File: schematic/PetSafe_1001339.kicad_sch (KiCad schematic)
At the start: 148 parts, among them J1 ICSP, J3 PIR BOARD, J5 MOTOR, J6 DNP, Q1 FMOS3401A?, Q11 MMBTA55?, Q2 BC847B?, Q3 MMBTA55?, Q4 MMBTA55?, Q5 MMBTA55?, Q6 MMBTA55?, Q7 BC857C?, Q8 SIL3724A?, Q9 NPN option / DNP, U1 S-1200B45?, U106 U6A / LDO option, U2 SN74LVC2G14DBV?, U3 SGM8542XS, U4 PIC16F18855, U5 MX512H, U6 S-812C33AMC? / 3.3V, U7 DNP, Y1 20 MHz

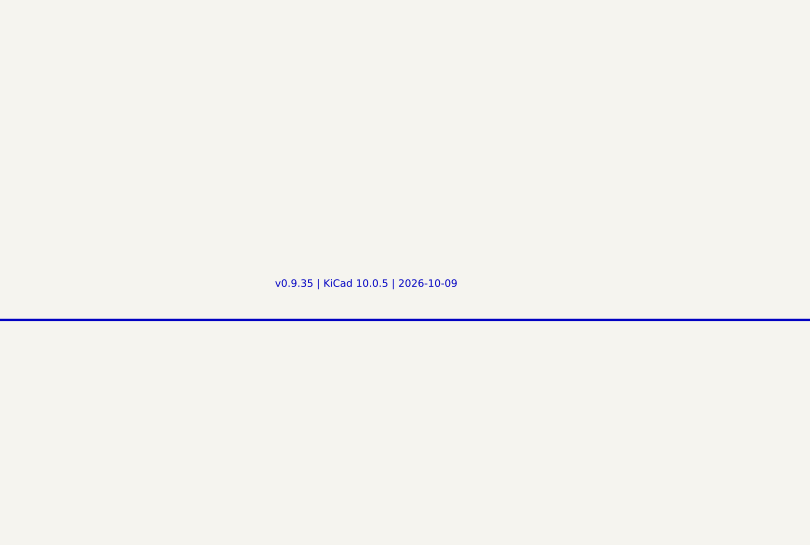
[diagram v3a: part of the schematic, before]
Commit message: Map J5 contacts and stage targeted antenna measurements
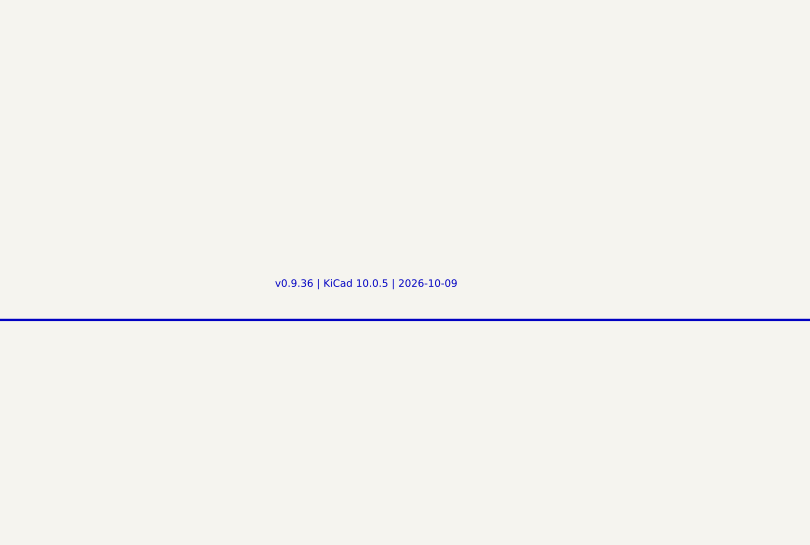
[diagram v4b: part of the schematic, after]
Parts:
- J5: CurrentEvidence (none) -> Photo-supported J5 map (IMG_2438 front, IMG_2439 rear): con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; Evidence Photo reconstruction; individual net evidence in reconstruc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 -> Photo-supported J5 map (IMG_2438 front, IMG_2439 rear): con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; PinMapping See evidence/pin_crosswalk.json; physical orientation may b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 -> Photo-supported J5 map (IMG_2438 front, IMG_2439 rear): con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
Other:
- note added: "v0.9.36 | KiCad 10.0.5 | 2026-10-09"
- note removed: "v0.9.35 | KiCad 10.0.5 | 2026-10-09"
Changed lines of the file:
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@@
 			)
 		)
+		(property "CurrentEvidence" "Photo-supported J5 map (IMG_2438 front, IMG_2439 rear): contact nearer C34 = A/native1 -> U5.8 OUTA; contact nearer BATTERY+ edge = B/native2 -> U5.5 OUTB/TP15. Connector body is on the rear. Harness colours, stock-footprint numbering and exact pitch remain unverified; no new bench result."
+			(at 499.11 62.23 0)
+			(effects
+				(font
+					(size 1.27 1.27)
+				)
+				(hide yes)
+			)
+		)
 		(pin "1"
 		)
@@
 				) hide)
 		)
-		(property "Evidence" "Photo reconstruction; individual net evidence in reconstruction.json"
+		(property "Evidence" "Photo-supported J5 map (IMG_2438 front, IMG_2439 rear): contact nearer C34 = A/native1 -> U5.8 OUTA; contact nearer BATTERY+ edge = B/native2 -> U5.5 OUTB/TP15. Connector body is on the rear. Harness colours, stock-footprint numbering and exact pitch remain unverified; no new bench result."
 			(at 499.11 62.23 0)
 			(effects
@@
 				) hide)
 		)
-		(property "PinMapping" "See evidence/pin_crosswalk.json; physical orientation may be provisional"
+		(property "PinMapping" "Photo-supported J5 map (IMG_2438 front, IMG_2439 rear): contact nearer C34 = A/native1 -> U5.8 OUTA; contact nearer BATTERY+ edge = B/native2 -> U5.5 OUTB/TP15. Connector body is on the rear. Harness colours, stock-footprint numbering and exact pitch remain unverified; no new bench result."
 			(at 499.11 62.23 0)
 			(effects
@@
 		)
 	)
-	(text "v0.9.35 | KiCad 10.0.5 | 2026-10-09"
+	(text "v0.9.36 | KiCad 10.0.5 | 2026-10-09"
 		(at 514.35 370.84000000000003 0)
 		(effects
@@
 	)
 	(junction
-		(at 430.53 87.63)
+		(at 455.93 87.63)
 		(diameter 0)
 		(color 0 0 0 0)
 	)
 	(junction
-		(at 455.93 87.63)
+		(at 461.01 87.63)
 		(diameter 0)
 		(color 0 0 0 0)
 	)
 	(junction
-		(at 114.3 298.45)
+		(at 330.2 326.39)
 		(diameter 0)
 		(color 0 0 0 0)
 	)
 	(junction
-		(at 330.2 326.39)
+		(at 262.89 132.08)
 		(diameter 0)
 		(color 0 0 0 0)
 	)
 	(junction
-		(at 55.88 81.28)
+		(at 302.26 132.08)
 		(diameter 0)
 		(color 0 0 0 0)
 	)
 	(junction
-		(at 83.82 81.28)
+		(at 114.3 81.28)
 		(diameter 0)
 		(color 0 0 0 0)
 	)
 	(junction
-		(at 262.89 132.08)
+		(at 430.53 87.63)
 		(diameter 0)
 		(color 0 0 0 0)
 	)
 	(junction
-		(at 302.26 132.08)
+		(at 55.88 81.28)
 		(diameter 0)
 		(color 0 0 0 0)
 	)
 	(junction
-		(at 461.01 87.63)
+		(at 528.32 87.63)
 		(diameter 0)
 		(color 0 0 0 0)
 	)
 	(junction
-		(at 114.3 81.28)
+		(at 342.9 52.07)
 		(diameter 0)
 		(color 0 0 0 0)
 	)
 	(junction
-		(at 342.9 52.07)
+		(at 213.36 364.49)
 		(diameter 0)
 		(color 0 0 0 0)
@@
 	)
 	(junction
-		(at 134.62 81.28)
+		(at 220.98 298.45)
 		(diameter 0)
 		(color 0 0 0 0)
 	)
 	(junction
-		(at 220.98 298.45)
+		(at 134.62 81.28)
 		(diameter 0)
 		(color 0 0 0 0)
 	)
 	(junction
-		(at 99.06 298.45)
+		(at 152.4 298.45)
 		(diameter 0)
 		(color 0 0 0 0)
@@
 	)
 	(junction
-		(at 213.36 364.49)
+		(at 259.08 298.45)
 		(diameter 0)
 		(color 0 0 0 0)
 	)
 	(junction
-		(at 259.08 298.45)
+		(at 114.3 298.45)
 		(diameter 0)
 		(color 0 0 0 0)
 	)
 	(junction
-		(at 152.4 298.45)
+		(at 60.96 298.45)
 		(diameter 0)
 		(color 0 0 0 0)
 	)
 	(junction
-		(at 60.96 298.45)
+		(at 83.82 81.28)
 		(diameter 0)
 		(color 0 0 0 0)
@@
 	)
 	(junction
-		(at 322.58 132.08)
+		(at 99.06 298.45)
 		(diameter 0)
 		(color 0 0 0 0)
 	)
 	(junction
-		(at 528.32 87.63)
+		(at 322.58 132.08)
 		(diameter 0)
 		(color 0 0 0 0)
 	)
 	(junction
-		(at 445.77 250.19)
+		(at 481.33 104.14)
 		(diameter 0)
 		(color 0 0 0 0)
 	)
 	(junction
-		(at 360.68 198.12)
+		(at 114.3 53.34)
 		(diameter 0)
 		(color 0 0 0 0)
 	)
 	(junction
-		(at 502.92 180.34)
+		(at 134.62 53.34)
 		(diameter 0)
 		(color 0 0 0 0)
 	)
 	(junction
-		(at 502.92 200.66)
+		(at 322.58 113.03)
 		(diameter 0)
 		(color 0 0 0 0)
 	)
 	(junction
-		(at 106.68 322.58)
+		(at 22.86 210.82)
 		(diameter 0)
 		(color 0 0 0 0)
 	)
 	(junction
-		(at 322.58 113.03)
+		(at 22.86 226.06)
 		(diameter 0)
 		(color 0 0 0 0)
 	)
 	(junction
-		(at 114.3 53.34)
+		(at 22.86 251.46)
 		(diameter 0)
 		(color 0 0 0 0)
 	)
 	(junction
-		(at 134.62 53.34)
+		(at 300.99 182.88)
 		(diameter 0)
 		(color 0 0 0 0)
 	)
 	(junction
-		(at 123.19 102.87)
+		(at 314.96 302.26)
 		(diameter 0)
 		(color 0 0 0 0)
 	)
 	(junction
-		(at 101.6 102.87)
+		(at 388.62 327.66)
 		(diameter 0)
 		(color 0 0 0 0)
 	)
 	(junction
-		(at 91.44 102.87)
+		(at 349.25 182.88)
 		(diameter 0)
 		(color 0 0 0 0)
 	)
 	(junction
-		(at 488.95 237.49)
+		(at 266.7 322.58)
 		(diameter 0)
 		(color 0 0 0 0)
 	)
 	(junction
-		(at 48.26 53.34)
+		(at 483.87 69.85)
 		(diameter 0)
 		(color 0 0 0 0)
 	)
 	(junction
-		(at 55.88 53.34)
+		(at 488.95 237.49)
 		(diameter 0)
 		(color 0 0 0 0)
 	)
 	(junction
-		(at 66.04 53.34)
+		(at 106.68 322.58)
 		(diameter 0)
 		(color 0 0 0 0)
 	)
 	(junction
-		(at 349.25 182.88)
+		(at 67.31 217.17)
 		(diameter 0)
 		(color 0 0 0 0)
 	)
 	(junction
-		(at 53.34 322.58)
+		(at 38.1 217.17)
 		(diameter 0)
 		(color 0 0 0 0)
 	)
 	(junction
-		(at 300.99 182.88)
+		(at 360.68 198.12)
 		(diameter 0)
 		(color 0 0 0 0)
 	)
 	(junction
-		(at 302.26 113.03)
+		(at 445.77 250.19)
 		(diameter 0)
 		(color 0 0 0 0)
 	)
 	(junction
-		(at 481.33 104.14)
+		(at 48.26 53.34)
 		(diameter 0)
 		(color 0 0 0 0)
 	)
 	(junction
-		(at 558.8 58.42)
+		(at 55.88 53.34)
 		(diameter 0)
 		(color 0 0 0 0)
 	)
 	(junction
-		(at 213.36 322.58)
+		(at 66.04 53.34)
 		(diameter 0)
 		(color 0 0 0 0)
 	)
 	(junction
-		(at 388.62 327.66)
+		(at 91.44 102.87)
 		(diameter 0)
 		(color 0 0 0 0)
 	)
 	(junction
-		(at 22.86 210.82)
+		(at 101.6 102.87)
 		(diameter 0)
 		(color 0 0 0 0)
 	)
 	(junction
-		(at 22.86 226.06)
+		(at 123.19 102.87)
 		(diameter 0)
 		(color 0 0 0 0)
 	)
 	(junction
-		(at 22.86 251.46)
+		(at 213.36 322.58)
 		(diameter 0)
 		(color 0 0 0 0)
 	)
 	(junction
-		(at 377.19 231.14)
+		(at 237.49 167.64)
 		(diameter 0)
 		(color 0 0 0 0)
 	)
 	(junction
-		(at 469.9 180.34)
+		(at 302.26 113.03)
 		(diameter 0)
 		(color 0 0 0 0)
 	)
 	(junction
-		(at 469.9 203.2)
+		(at 469.9 180.34)
 		(diameter 0)
 		(color 0 0 0 0)
 	)
 	(junction
-		(at 67.31 185.42)
+		(at 469.9 203.2)
 		(diameter 0)
 		(color 0 0 0 0)
@@
 	)
 	(junction
-		(at 237.49 167.64)
+		(at 67.31 185.42)
 		(diameter 0)
 		(color 0 0 0 0)
 	)
 	(junction
-		(at 236.22 114.3)
+		(at 558.8 58.42)
 		(diameter 0)
 		(color 0 0 0 0)
 	)
 	(junction
-		(at 38.1 217.17)
+		(at 355.6 306.07)
 		(diameter 0)
 		(color 0 0 0 0)
 	)
 	(junction
-		(at 67.31 217.17)
+		(at 368.3 306.07)
 		(diameter 0)
 		(color 0 0 0 0)
 	)
 	(junction
-		(at 314.96 302.26)
+		(at 398.78 200.66)
 		(diameter 0)
 		(color 0 0 0 0)
 	)
 	(junction
-		(at 266.7 322.58)
+		(at 398.78 180.34)
 		(diameter 0)
 		(color 0 0 0 0)
 	)
 	(junction
-		(at 363.22 203.2)
+		(at 53.34 322.58)
 		(diameter 0)
 		(color 0 0 0 0)
 	)
 	(junction
-		(at 363.22 180.34)
+		(at 377.19 231.14)
 		(diameter 0)
 		(color 0 0 0 0)
@@
 	)
 	(junction
-		(at 368.3 306.07)
+		(at 351.79 345.44)
 		(diameter 0)
 		(color 0 0 0 0)
 	)
 	(junction
-		(at 355.6 306.07)
+		(at 363.22 203.2)
 		(diameter 0)
 		(color 0 0 0 0)
 	)
 	(junction
-		(at 483.87 69.85)
+		(at 363.22 180.34)
 		(diameter 0)
 		(color 0 0 0 0)
 	)
 	(junction
-		(at 160.02 322.58)
+		(at 502.92 200.66)
 		(diameter 0)
 		(color 0 0 0 0)
 	)
 	(junction
-		(at 398.78 200.66)
+		(at 502.92 180.34)
 		(diameter 0)
 		(color 0 0 0 0)
 	)
 	(junction
-		(at 398.78 180.34)
+		(at 160.02 322.58)
 		(diameter 0)
 		(color 0 0 0 0)
 	)
 	(junction
-		(at 351.79 345.44)
+		(at 236.22 114.3)
 		(diameter 0)
 		(color 0 0 0 0)
@@
 		)
 	)
-	(label "H_BAT_SENSE"
-		(at 355.6 90.17 0)
+	(label "VREF"
+		(at 464.82 198.12 0)
 		(effects
 			(font
@@
 	)
 	(label "H_BAT_SENSE"
-		(at 375.92 95.25 0)
+		(at 355.6 90.17 0)
 		(effects
 			(font
@@
 		)
 	)
-	(label "VREF"
-		(at 464.82 198.12 0)
+	(label "H_BAT_SENSE"
+		(at 375.92 95.25 0)
 		(effects
 			(font
@@
 		(title "PetSafe 100-1339 R03 A | single-sheet reconstruction")
 		(date "2026-10-09")
-		(rev "0.9.35")
+		(rev "0.9.36")
 		(company "KiCad 10 libraries + four datasheet symbols | MCP authoring")
-		(comment 1 "LED1 channels verified: R30 red; R31 green. Package map qualified.")
+		(comment 1 "J5 board contacts mapped from photos. Antenna topology remains under review.")
 	)
 )

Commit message: Correct front antenna capacitor band using measured C11 continuity
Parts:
- C11: CurrentEvidence (none) -> v0.9.37: Measured C11.1-ANT2 = 1.4 ohm (B52). Pin1 is ANT2/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; Evidence Photo reconstruction; individual net evidence in reconstruc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 -> v0.9.37: Measured C11.1-ANT2 = 1.4 ohm (B52). Pin1 is ANT2/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; ViaEvidence v0.9: pin1 ground return from user-reviewed via/photo compa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 -> v0.9.37: former front-band association to V087/V088 withdra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
- C14, C29, C44, C47: CurrentEvidence (none) -> v0.9.37: IMG_2433 shows its outer pad on the same continuou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; Evidence Photo reconstruction; individual net evidence in reconstruc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 -> v0.9.37: IMG_2433 shows its outer pad on the same continuou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; ViaEvidence v0.9: pin1 ground return from user-reviewed via/photo compa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 -> v0.9.37: former front-band association to V087/V088 withdra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
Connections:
- net GND: no longer C11.1, C14.1, C29.1, C44.1, C47.1
- net H_ANT_B: now also C11.1, C14.1, C29.1, C44.1, C47.1
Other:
- note added: "Front outer-capacitor band = ANT2: C11 measured 1.4 ohm; other four share visible copper."
- note added: "Rear capacitor returns remain GND. Front and rear capacitors are not drawn in parallel."
- note added: "v0.9.37 | KiCad 10.0.5 | 2026-10-14"
- note removed: "Local three-capacitor junctions retained. Hidden links from these midpoints to antenna remain unknown."
- note removed: "v0.9.36 | KiCad 10.0.5 | 2026-10-09"
- note removed: "v0.9: user-reviewed GND returns replace previous antenna rails on this capacitor bank."

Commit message: Resolve RA0 receiver link and TP14 motor output in v0.9.39
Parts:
- C25, TP6: CurrentEvidence (none) -> v0.9.38: B59 C25.1 to TP6.1 = 1.5 ohm unpowered supports PI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; Evidence Photo reconstruction; individual net evidence in reconstruc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 -> v0.9.38: B59 C25.1 to TP6.1 = 1.5 ohm unpowered supports PI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; RA0Evidence (none) -> v0.9.38: B59 C25.1 to TP6.1 = 1.5 ohm unpowered supports PI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
- C27, C33, R3, R44, TP107: ViaEvidence v0.9.9: User corrects raw battery+ versus post-Q1 rail. BATP -> Q1.S (single physical pad/native3, candidate drain); Q1.L/native2 (candidate source) -> U5.4/V011-V014. These are distinct copper nets, connected through Q1. IMG_2438 also supports TP14 on battery+; V015/R43.2-TP14 user confirmation retained. Q1.R/native1 is candidate gate at R44.2. Photo S means SINGLE, not MOSFET source. -> v0.9.9: User corrects raw battery+ versus post-Q1 rail. BATP -> Q1.S (single physical pad/native3, candidate drain); Q1.L/native2 (candidate source) -> U5.4/V011-V014. These are distinct copper nets, connected through Q1. TP14/R43.2/V015 is OUTA/H_MOTOR_A, supported by TP14-U5.8 = 1.5 ohm; the earlier battery-side photo interpretation is withdrawn. Q1.R/native1 is candidate gate at R44.2. Photo S means SINGLE, not MOSFET source.
- Q1: CurrentEvidence R1A marking matches Formosa FMOS3401A datasheet p5; SOT-23 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 -> v0.9.39: TP14 to MX512H/U5 pin8 = 1.5 ohm supports OUTA/H_M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; Evidence R1A marking matches Formosa FMOS3401A datasheet p5; SOT-23 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 -> v0.9.39: TP14 to MX512H/U5 pin8 = 1.5 ohm supports OUTA/H_M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; TP14Evidence (none) -> v0.9.39: TP14 to MX512H/U5 pin8 = 1.5 ohm supports OUTA/H_M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; ViaEvidence v0.9.9: User corrects raw battery+ versus post-Q1 rail. BATP -> Q1.S (single physical pad/native3, candidate drain); Q1.L/native2 (candidate source) -> U5.4/V011-V014. These are distinct copper nets, connected through Q1. IMG_2438 also supports TP14 on battery+; V015/R43.2-TP14 user confirmation retained. Q1.R/native1 is candidate gate at R44.2. Photo S means SINGLE, not MOSFET source. -> v0.9.9: User corrects raw battery+ versus post-Q1 rail. BATP -> Q1.S (single physical pad/native3, candidate drain); Q1.L/native2 (candidate source) -> U5.4/V011-V014. These are distinct copper nets, connected through Q1. TP14/R43.2/V015 is OUTA/H_MOTOR_A, supported by TP14-U5.8 = 1.5 ohm; the earlier battery-side photo interpretation is withdrawn. Q1.R/native1 is candidate gate at R44.2. Photo S means SINGLE, not MOSFET source.
- R43, TP14: CurrentEvidence (none) -> v0.9.39: TP14 to MX512H/U5 pin8 = 1.5 ohm supports OUTA/H_M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; Evidence Photo reconstruction; individual net evidence in reconstruc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 -> v0.9.39: TP14 to MX512H/U5 pin8 = 1.5 ohm supports OUTA/H_M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; TP14Evidence (none) -> v0.9.39: TP14 to MX512H/U5 pin8 = 1.5 ohm supports OUTA/H_M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; ViaEvidence v0.9.9: User corrects raw battery+ versus post-Q1 rail. BAT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 -> V015 joins R43.2 and TP14. User TP14-U5.8 = 1.5 ohm resolve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
- U4: CurrentEvidence (none) -> v0.9.38: B59 C25.1 to TP6.1 = 1.5 ohm unpowered supports PI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; Evidence Photo reconstruction; individual net evidence in reconstruc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 -> v0.9.38: B59 C25.1 to TP6.1 = 1.5 ohm unpowered supports PI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; RA0Evidence (none) -> v0.9.38: B59 C25.1 to TP6.1 = 1.5 ohm unpowered supports PI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; UserGPIOEvidence v0.8: user confirms multimeter + visual trace. 3-TP7/R28/R2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 -> Measured and photo-supported destinations are recorded in p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
- U5: CurrentEvidence (none) -> v0.9.39: TP14 to MX512H/U5 pin8 = 1.5 ohm supports OUTA/H_M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; Evidence Photo reconstruction; individual net evidence in reconstruc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 -> v0.9.39: TP14 to MX512H/U5 pin8 = 1.5 ohm supports OUTA/H_M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; TP14Evidence (none) -> v0.9.39: TP14 to MX512H/U5 pin8 = 1.5 ohm supports OUTA/H_M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; ViaEvidence v0.9.9: User corrects raw battery+ versus post-Q1 rail. BATP -> Q1.S (single physical pad/native3, candidate drain); Q1.L/native2 (candidate source) -> U5.4/V011-V014. These are distinct copper nets, connected through Q1. IMG_2438 also supports TP14 on battery+; V015/R43.2-TP14 user confirmation retained. Q1.R/native1 is candidate gate at R44.2. Photo S means SINGLE, not MOSFET source. -> v0.9.9: User corrects raw battery+ versus post-Q1 rail. BATP -> Q1.S (single physical pad/native3, candidate drain); Q1.L/native2 (candidate source) -> U5.4/V011-V014. These are distinct copper nets, connected through Q1. TP14/R43.2/V015 is OUTA/H_MOTOR_A, supported by TP14-U5.8 = 1.5 ohm; the earlier battery-side photo interpretation is withdrawn. Q1.R/native1 is candidate gate at R44.2. Photo S means SINGLE, not MOSFET source.
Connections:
- net BATTERY+: no longer R43.2, TP14.1
- net H_MOTOR_A: now reaches J5.1 (Pin_1), U5.8 (OUTA)
- net H_MOTOR_A: now also R43.2, TP14.1
- net RX_A_FILTER: now reaches C25.1, U4.2 (RA0)
- net RX_A_FILTER: now also C18.2, R27.1, TP6.1
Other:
- note added: "RA0 reaches TP6 (B59). TP11/TP17 onward paths remain qualified."
- note added: "TP14 / R43.2 = OUTA / U5 pin8: measured 1.5 ohm. Separate from BATTERY+."
- note added: "U6: pin5 joins VIN (1 ohm); pin4 unused. PIR supply measured 3.3 V with sensor attached."
- note added: "VDD / TP103: logic supply measured 4.5 V (B56, red-blinking state). V082 confirmed here."
- note added: "v0.9.39 | KiCad 10.0.5 | 2026-10-14"
- note removed: "PIC pads have local nets; some onward routes remain unresolved."
- note removed: "U5 alternative: DRV8212PDSGR. Different package/pins; redesign required."
- note removed: "U6: pin5 joins VIN (1 ohm); pin4 unused by user/photo. 3.3V is candidate rating."
- note removed: "VDD / TP103: regulated logic supply VDD; candidate 4.5V, not measured. V082 confirmed here."
- note removed: "v0.9.37 | KiCad 10.0.5 | 2026-10-14"

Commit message: Record Q7 junction and rest bias evidence; investigate U2 supply
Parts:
- Q7: CurrentEvidence 3GW supports BC857C PNP. Photo and 11.2 kohm R18+R19 path s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 -> B65/B66 confirm Q7.L-R19.1 and Q7.R-R19.2 at 1.5 ohm. B67-B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; Evidence 3GW supports BC857C PNP. Photo and 11.2 kohm R18+R19 path s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 -> B65/B66 confirm Q7.L-R19.1 and Q7.R-R19.2 at 1.5 ohm. B67-B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
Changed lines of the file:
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@@
 			)
 		)
-		(property "CurrentEvidence" "3GW supports BC857C PNP. Photo and 11.2 kohm R18+R19 path support B=L, E=R/VDD, C=S/R20; terminal selection and switching role remain inferred. Control input R18.1 is now user-confirmed to PIC12/RC1 via V053-V070."
+		(property "CurrentEvidence" "B65/B66 confirm Q7.L-R19.1 and Q7.R-R19.2 at 1.5 ohm. B67-B70 diode polarity supports PNP/base at L; R=emitter/S=collector remains the 3GW/BC857C datasheet/circuit assignment, not a unique diode-test result. B71 direct V(R)-V(L)=0 V is consistent with no forward base-emitter bias in the latest powered state; this fits low TP5/VREF. Earlier separate R19 0/4.5 V readings remain conflicting history, not a failure diagnosis. Exact part, switching pulses and enabled-state behavior remain unverified."
 			(at 313.69 182.88 0)
 			(effects
@@
 				) hide)
 		)
-		(property "Evidence" "3GW supports BC857C PNP. Photo and 11.2 kohm R18+R19 path support B=L, E=R/VDD, C=S/R20; terminal selection and switching role remain inferred. Control input R18.1 is now user-confirmed to PIC12/RC1 via V053-V070."
+		(property "Evidence" "B65/B66 confirm Q7.L-R19.1 and Q7.R-R19.2 at 1.5 ohm. B67-B70 diode polarity supports PNP/base at L; R=emitter/S=collector remains the 3GW/BC857C datasheet/circuit assignment, not a unique diode-test result. B71 direct V(R)-V(L)=0 V is consistent with no forward base-emitter bias in the latest powered state; this fits low TP5/VREF. Earlier separate R19 0/4.5 V readings remain conflicting history, not a failure diagnosis. Exact part, switching pulses and enabled-state behavior remain unverified."
 			(at 313.69 182.88 0)
 			(effects

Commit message: Correct U2 supply through R5 and reconcile RF output evidence
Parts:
- C7: CurrentEvidence (none) -> Upper/model1 shares U2 pin5 supply at 1.5 ohm (B78); R5 sup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; Evidence Photo reconstruction; individual net evidence in reconstruc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 -> Upper/model1 shares U2 pin5 supply at 1.5 ohm (B78); R5 sup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
- Q8: CurrentEvidence 3724A supports the SIL3724A complementary MOSFET candidate;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 -> 3724A supports SIL3724A complementary MOSFET candidate; fit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; Evidence 3724A supports the SIL3724A complementary MOSFET candidate;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 -> 3724A supports SIL3724A complementary MOSFET candidate; fit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
- R5: CurrentEvidence (none) -> Marking 220 = 22 ohm. B80 C7 upper-R5 upper = 4 ohm; B81 C6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; Evidence Photo reconstruction; individual net evidence in reconstruc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 -> Marking 220 = 22 ohm. B80 C7 upper-R5 upper = 4 ohm; B81 C6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
- TP105: CurrentEvidence (none) -> Q8 joined outer drain/output pads reach ANT1 by photo-suppo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; Evidence Photo reconstruction; individual net evidence in reconstruc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 -> Q8 joined outer drain/output pads reach ANT1 by photo-suppo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
- U2: Evidence Photo reconstruction; individual net evidence in reconstruc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 -> C14R / SN74LVC2G14 remains a candidate. B76 supply-to-groun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
- U2: CurrentEvidence (none) -> C14R / SN74LVC2G14 remains a candidate. B76 supply-to-groun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; Evidence Photo reconstruction; individual net evidence in reconstruc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 -> C14R / SN74LVC2G14 remains a candidate. B76 supply-to-groun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
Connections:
- net H_ANT_A: now also Q8.4 (D), Q8.6 (D); no longer R5.2
- net H_RF_VDD: now also R5.1
- net VDD: no longer C7.1, U2.5 (VCC)
- new net U2_VCC: C7.1, R5.2, U2.5 (VCC)
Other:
- note added: "H07: RF supply -> R5 (22 ohm) -> U2/C7. U2 measured 6.3 V; candidate rating unresolved."
- note added: "Q8 output -> ANT1 photo-supported (B82: 4.5 ohm). Rest VGS: P=0 V, N=6.3 V; scope deferred."
- note added: "v0.9.40 | KiCad 10.0.5 | 2026-10-15"
- note removed: "C6 parallels C5 (photo); Q8 P-F = 1 ohm supports H_RF_VDD join. Gate drive unverified."
- note removed: "H07: C14R inverter candidate. C6 parallels C5 by photo; Q8 source rail supported by B37."
- note removed: "v0.9.39 | KiCad 10.0.5 | 2026-10-14"
- moved on the sheet: R5
